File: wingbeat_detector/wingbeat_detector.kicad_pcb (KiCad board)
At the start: 4 copper layers, 36 x 18 mm, 54 parts, among them J1 USB_C_10137062-00021LF, J2 CONN_UMC_JACK_SMD, J3 CONN_UMC_JACK_SMD, J4 CONN_UMC_JACK_SMD, Q1 MOSFET-N-CH, U1 MAX865EUA+, U2 UAF42_SMA, U3 UAF42_SMA, U4 OPA381, U5 TSV630IQ1T, U6 LED_DRV_50mA

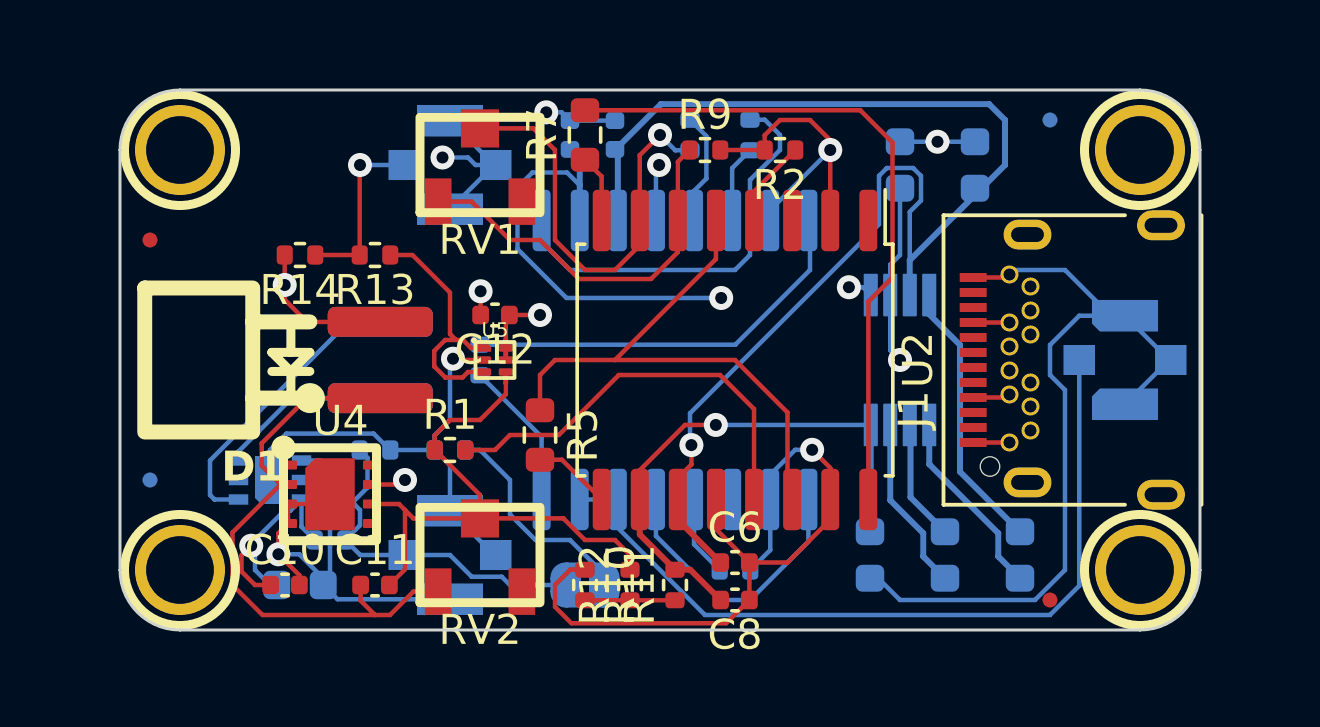
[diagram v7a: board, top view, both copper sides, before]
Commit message: Fill zones, no errors
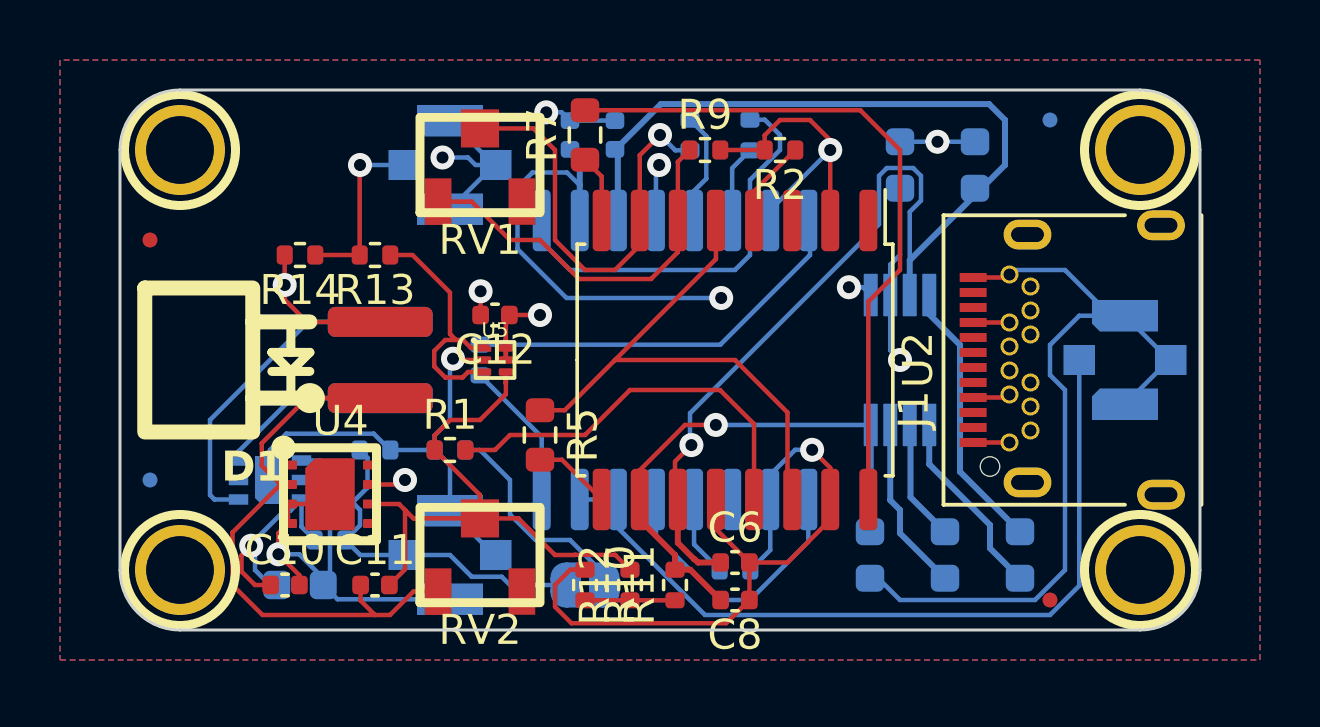
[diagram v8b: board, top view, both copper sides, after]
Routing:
- net Net-(D2-A): track 8.70 -> 9.49 mm
- net Net-(U2-Vin1): track 14.1 -> 13.4 mm
- net /filter/HIGHPASS: track 19.3 -> 18.6 mm
- net /V10+: track 43.6 -> 44.1 mm
- added copper zone on B.Cu, net /GND
- added copper zone on F.Cu, net /GND
